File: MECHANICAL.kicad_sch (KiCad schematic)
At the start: 16 parts

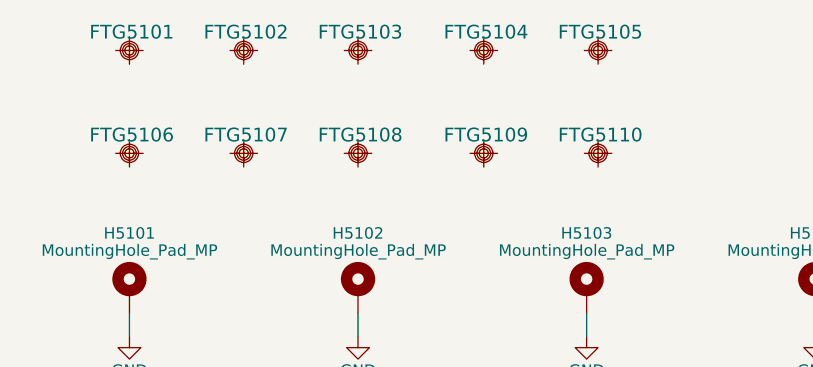
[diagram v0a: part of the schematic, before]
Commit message: New channels topolgy added
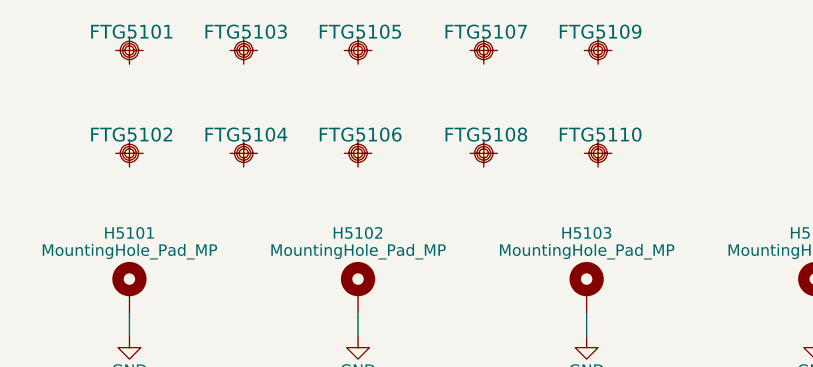
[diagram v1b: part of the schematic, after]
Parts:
- renumbered FTG5106 to FTG5102, FTG5102 to FTG5103, FTG5107 to FTG5104, FTG5103 to FTG5105, FTG5108 to FTG5106, FTG5104 to FTG5107, FTG5109 to FTG5108, FTG5105 to FTG5109
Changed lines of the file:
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@@
 		(on_board yes)
 		(dnp no)
-		(property "Reference" "FTG5102"
+		(property "Reference" "FTG5103"
 			(at 114.554 48.768 0)
 			(effects
@@
 			(project ""
 				(path "/41597329-5145-432a-9041-5bc2cec82d9b/18acdedb-eb6b-4543-994d-80b3dce360be"
-					(reference "FTG5102")
+					(reference "FTG5103")
 					(unit 1)
 				)
@@
 		(on_board yes)
 		(dnp no)
-		(property "Reference" "FTG5104"
+		(property "Reference" "FTG5107"
 			(at 141.224 48.768 0)
 			(effects
@@
 			(project ""
 				(path "/41597329-5145-432a-9041-5bc2cec82d9b/18acdedb-eb6b-4543-994d-80b3dce360be"
-					(reference "FTG5104")
+					(reference "FTG5107")
 					(unit 1)
 				)
@@
 		(on_board yes)
 		(dnp no)
-		(property "Reference" "FTG5106"
+		(property "Reference" "FTG5102"
 			(at 101.854 60.198 0)
 			(effects
@@
 			(project ""
 				(path "/41597329-5145-432a-9041-5bc2cec82d9b/18acdedb-eb6b-4543-994d-80b3dce360be"
-					(reference "FTG5106")
+					(reference "FTG5102")
 					(unit 1)
 				)
@@
 		(on_board yes)
 		(dnp no)
-		(property "Reference" "FTG5103"
+		(property "Reference" "FTG5105"
 			(at 127.254 48.768 0)
 			(effects
@@
 			(project ""
 				(path "/41597329-5145-432a-9041-5bc2cec82d9b/18acdedb-eb6b-4543-994d-80b3dce360be"
-					(reference "FTG5103")
+					(reference "FTG5105")
 					(unit 1)
 				)
@@
 		(on_board yes)
 		(dnp no)
-		(property "Reference" "FTG5109"
+		(property "Reference" "FTG5108"
 			(at 141.224 60.198 0)
 			(effects
@@
 			(project ""
 				(path "/41597329-5145-432a-9041-5bc2cec82d9b/18acdedb-eb6b-4543-994d-80b3dce360be"
-					(reference "FTG5109")
+					(reference "FTG5108")
 					(unit 1)
 				)
@@
 		(on_board yes)
 		(dnp no)
-		(property "Reference" "FTG5108"
+		(property "Reference" "FTG5106"
 			(at 127.254 60.198 0)
 			(effects
@@
 			(project ""
 				(path "/41597329-5145-432a-9041-5bc2cec82d9b/18acdedb-eb6b-4543-994d-80b3dce360be"
-					(reference "FTG5108")
+					(reference "FTG5106")
 					(unit 1)
 				)
@@
 		(on_board yes)
 		(dnp no)
-		(property "Reference" "FTG5105"
+		(property "Reference" "FTG5109"
 			(at 153.924 48.768 0)
 			(effects
@@
 			(project ""
 				(path "/41597329-5145-432a-9041-5bc2cec82d9b/18acdedb-eb6b-4543-994d-80b3dce360be"
-					(reference "FTG5105")
+					(reference "FTG5109")
 					(unit 1)
 				)
@@
 		(on_board yes)
 		(dnp no)
-		(property "Reference" "FTG5107"
+		(property "Reference" "FTG5104"
 			(at 114.554 60.198 0)
 			(effects
@@
 			(project ""
 				(path "/41597329-5145-432a-9041-5bc2cec82d9b/18acdedb-eb6b-4543-994d-80b3dce360be"
-					(reference "FTG5107")
+					(reference "FTG5104")
 					(unit 1)
 				)

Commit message: WIP snapshot
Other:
- note added: "Fixme: Add bolts for heatsink"
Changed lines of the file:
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@@
 	(generator_version "9.0")
 	(paper "A3")
+	(text "Fixme: Add bolts for heatsink\n"
+		(exclude_from_sim no)
+		(at 115.062 115.062 0)
+		(effects
+			(font
+				(size 3.81 3.81)
+				(thickness 0.762)
+				(bold yes)
+				(color 255 0 0 1)
+			)
+		)
+	)
 	(wire
 		(pts

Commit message: Update project files and backups
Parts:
- removed H5101, H5102, H5103, H5104, H5105, H5106: MountingHole_Pad_MP, MountingHole:MountingHole_3.2mm_M3_DIN965_Pad_TopBottom, symbol Mechanical:MountingHole_Pad_MP
- added B5101, B5103, B5104, B5105, B5106, B5107, B5108, B5109, B5110, B5111, B5114, B5115, B5116, B5117: ${FAMILY}, Pads:MTG320_700V8P, symbol CERN:Pads/PLATED_HOLE3.2_PAD7.0_8VIA
- added R5101, R5102, R5103, R5104, R5105, R5106, R5109, R5110, R5111, R5112, R5113, R5115, R5116, R5117: 10, Resistors SMD:RESC3216X65N, symbol CERN:Resistors SMD/R1206_10R_1%_0.25W_100PPM
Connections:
- net GND: now also R5101.1, R5102.1, R5103.1, R5104.1, R5105.1, R5106.1, R5109.1, R5110.1, R5111.1, R5112.1, R5113.1, R5115.1, R5116.1, R5117.1
- new net: B5108.1, R5103.2
- new net: B5103.1, R5115.2
- new net: B5110.1, R5105.2
- new net: B5107.1, R5102.2
- new net: B5117.1, R5112.2
- new net: B5111.1, R5106.2
- new net: B5104.1, R5116.2
- new net: B5116.1, R5111.2
- new net: B5109.1, R5104.2
- new net: B5114.1, R5109.2
- new net: B5101.1, R5113.2
- new net: B5105.1, R5117.2
- new net: B5115.1, R5110.2
- new net: B5106.1, R5101.2
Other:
- note added: "HEATSINK"
- note removed: "Fixme: Add bolts for heatsink"
